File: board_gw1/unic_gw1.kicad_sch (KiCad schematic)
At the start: 112 parts, among them Q1 2N7002, Q10 2N7002, Q11 2N7002, Q12 2N7002, Q13 2N7002, Q14 2N7002, Q15 2N7002, Q16 2N7002, Q17 2N7002, Q18 2N7002, Q19 2N7002, Q2 2N7002, Q20 2N7002, Q21 2N7002, Q22 2N7002, Q23 2N7002, Q24 2N7002, Q25 2N7002, Q26 2N7002, Q27 2N7002, Q28 2N7002, Q29 2N7002, Q3 2N7002, Q30 2N7002, Q31 2N7002, Q32 2N7002, Q33 2N7002, Q34 2N7002, Q35 2N7002, Q36 2N7002, Q37 2N7002, Q38 2N7002, Q39 2N7002, Q4 2N7002, Q40 2N7002, Q5 2N7002, Q6 2N7002, Q7 2N7002, Q8 2N7002, Q9 2N7002, U1 GW1N-LV9QN88C6_I5_, U2 LM3480-3.3, U3 AP2202K-ADJ, U4 APS6404L-3SQR-ZR, U6 AP62150Z6, U7 W25Q16JVUXIQ, X1 27MHz

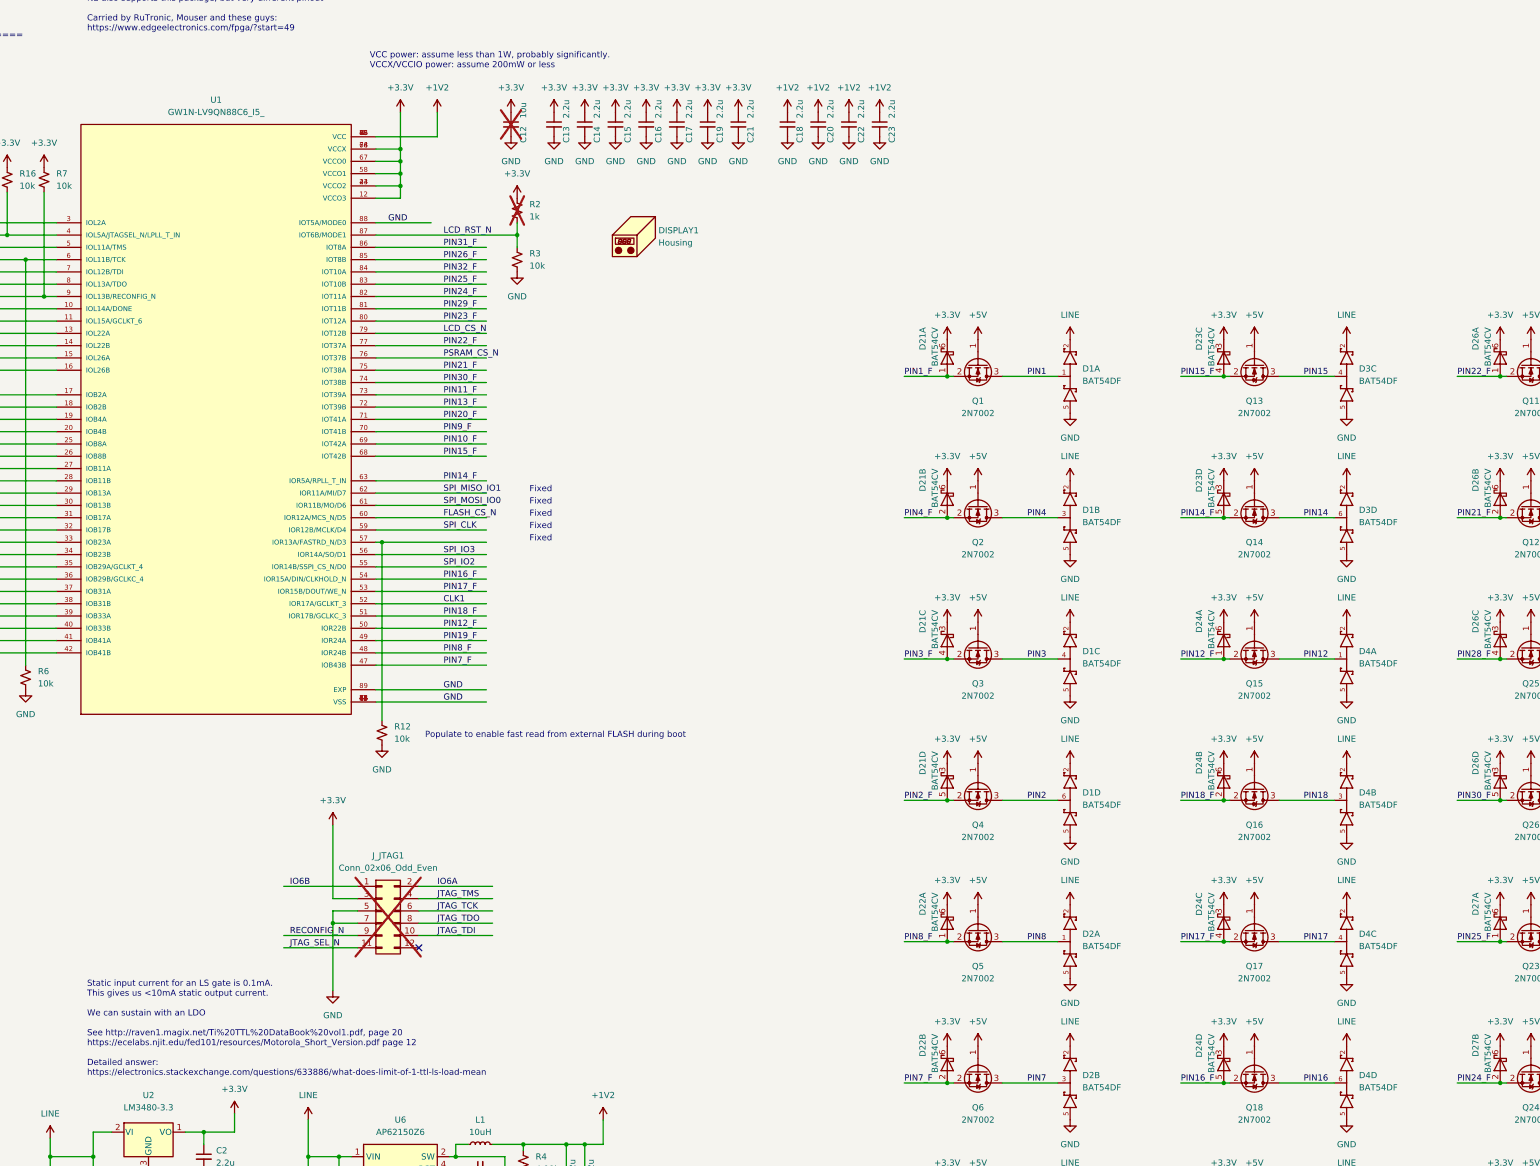
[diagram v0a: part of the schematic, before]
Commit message: Some updated to UNIC GW1 based on post-release learnings.
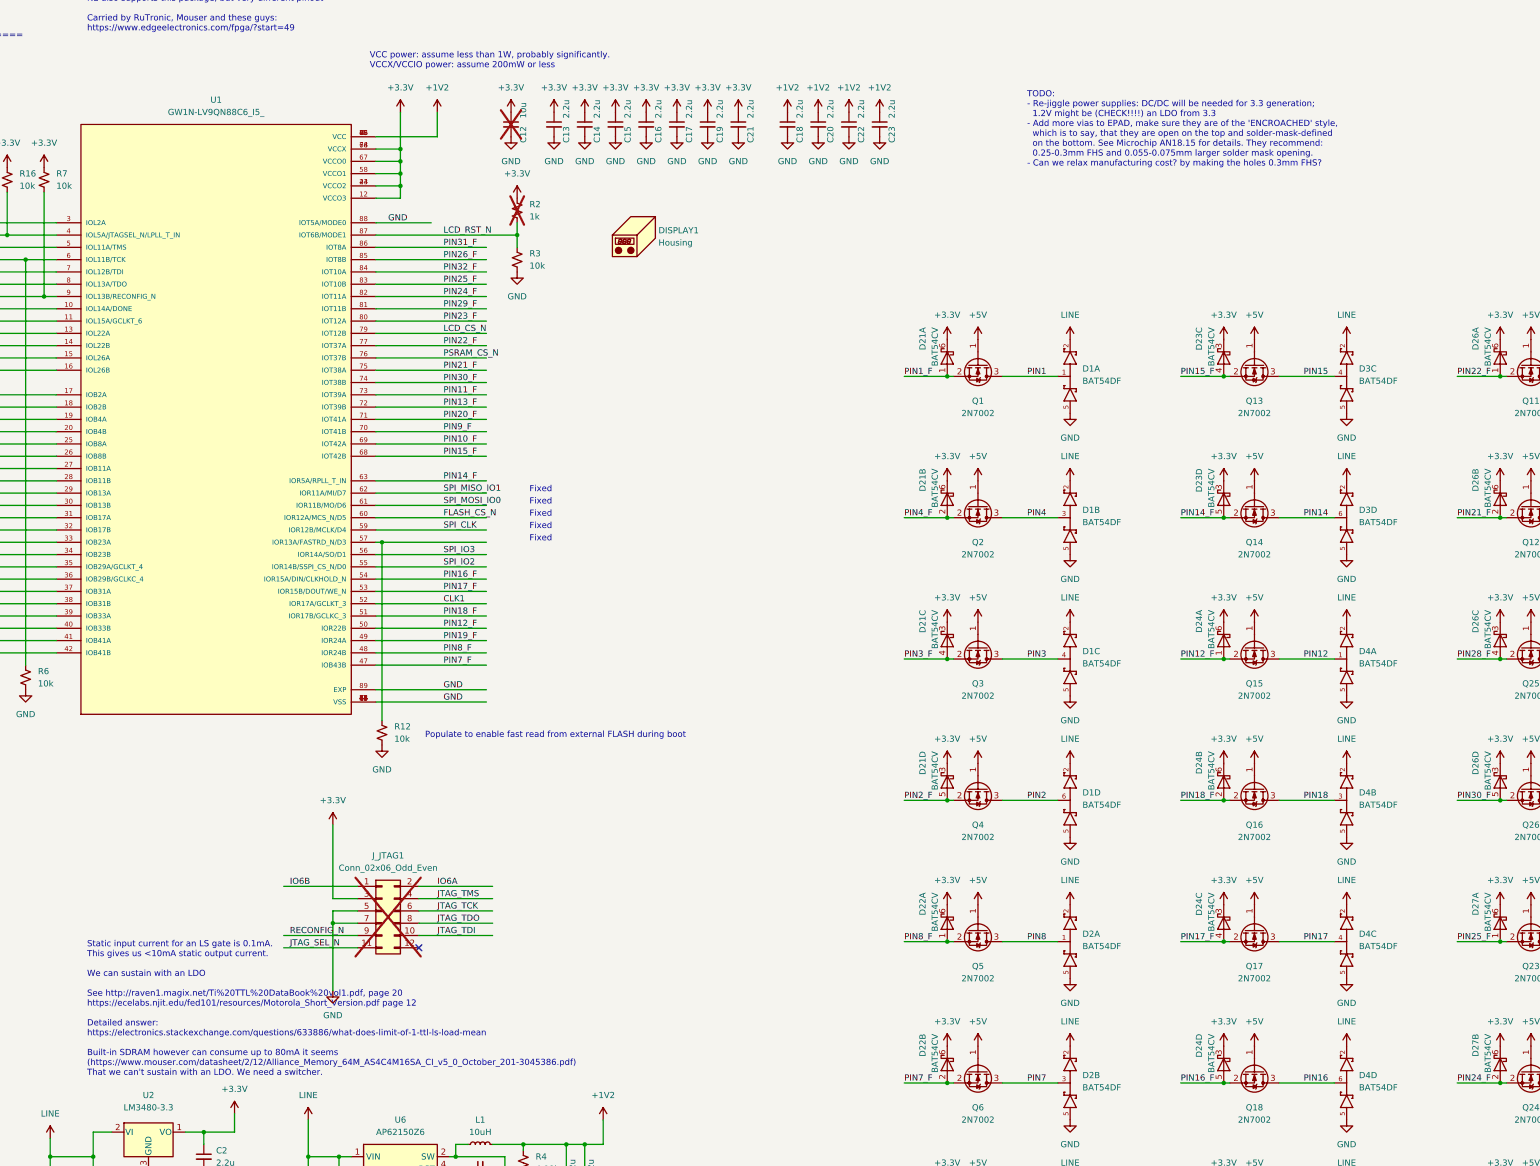
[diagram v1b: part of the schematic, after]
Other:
- note added: "Static input current for an LS gate is 0.1mA. This gives us <10mA static output current. We can sustain with an LDO See http://raven1.magix.net/Ti%20TTL%20DataBook%20vol1.pdf, page 20 https://ecelabs.njit.edu/fed101/resources/Motorola_Short_Version.pdf page 12 Detailed answer: https://electronics.stackexchange.com/questions/633886/what-does-limit-of-1-ttl-ls-load-mean Built-in SDRAM however can c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"
- note added: "TODO: - Re-jiggle power supplies: DC/DC will be needed for 3.3 generation; 1.2V might be (CHECK!!!!) an LDO from 3.3 - Add more vias to EPAD, make sure they are of the 'ENCROACHED' style, which is to say, that they are open on the top and solder-mask-defined on the bottom. See Microchip AN18.15 for details. They recommend: 0.25-0.3mm FHS and 0.055-0.075mm larger solder mask opening. - Can we rela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"
- note removed: "Static input current for an LS gate is 0.1mA. This gives us <10mA static output current. We can sustain with an LDO See http://raven1.magix.net/Ti%20TTL%20DataBook%20vol1.pdf, page 20 https://ecelabs.njit.edu/fed101/resources/Motorola_Short_Version.pdf page 12 Detailed answer: https://electronics.stackexchange.com/questions/633886/what-does-limit-of-1-ttl-ls-load-mean"
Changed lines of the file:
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@@
+    (effects (font (size 1.27 1.27)) (justify left bottom))
+  )
+  (text "TODO:\n- Re-jiggle power supplies: DC/DC will be needed for 3.3 generation;\n  1.2V might be (CHECK!!!!) an LDO from 3.3\n- Add more vias to EPAD, make sure they are of the 'ENCROACHED' style,\n  which is to say, that they are open on the top and solder-mask-defined\n  on the bottom. See Microchip AN18.15 for details. They recommend:\n  0.25-0.3mm FHS and 0.055-0.075mm larger solder mask opening.\n- Can we relax manufacturing cost? by making the holes 0.3mm FHS?"
+    (at 334.01 57.15 0)
     (effects (font (size 1.27 1.27)) (justify left bottom))
   )
@@
     (effects (font (size 1.27 1.27)) (justify left bottom))
   )
-  (text "Static input current for an LS gate is 0.1mA.\nThis gives us <10mA static output current.\n\nWe can sustain with an LDO\n\nSee http://raven1.magix.net/Ti%20TTL%20DataBook%20vol1.pdf, page 20\nhttps://ecelabs.njit.edu/fed101/resources/Motorola_Short_Version.pdf page 12\n\nDetailed answer:\nhttps://electronics.stackexchange.com/questions/633886/what-does-limit-of-1-ttl-ls-load-mean"
+  (text "Static input current for an LS gate is 0.1mA.\nThis gives us <10mA static output current.\n\nWe can sustain with an LDO\n\nSee http://raven1.magix.net/Ti%20TTL%20DataBook%20vol1.pdf, page 20\nhttps://ecelabs.njit.edu/fed101/resources/Motorola_Short_Version.pdf page 12\n\nDetailed answer:\nhttps://electronics.stackexchange.com/questions/633886/what-does-limit-of-1-ttl-ls-load-mean\n\nBuilt-in SDRAM however can consume up to 80mA it seems\n(https://www.mouser.com/datasheet/2/12/Alliance_Memory_64M_AS4C4M16SA_CI_v5_0_October_201-3045386.pdf)\nThat we can't sustain with an LDO. We need a switcher."
     (at 139.7 245.11 0)
     (effects (font (size 1.27 1.27)) (justify left bottom))
@@
       (effects (font (size 1.27 1.27)) (justify bottom) hide)
     )
-    (property "Description" "\nVolatile SRAM based and non-volatile flash-based field-programmable gate array (FPGA) technology\n" (at 166.37 109.22 0)
+    (property "Description" "Volatile SRAM based and non-volatile flash-based field-programmable gate array (FPGA) technology" (at 166.37 109.22 0)
       (effects (font (size 1.27 1.27)) (justify bottom) hide)
     )

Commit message: Updated board file; started cover CAD.
This checkin marks the hopefully complete V1.0 design for the form-factor
board.

It also contains the first (incomplete) iteration of the cover design.
It has a bunch of interference with components on the PCB which
needs to be cleaned. It's also unclear if snaps have to be 1.5mm thick.
Seems excessive. Finally, I don't think the OLED display can even survive
such stiff snaps. But it at least a start.
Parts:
- removed C12: 10u, Capacitor_SMD:C_0805_2012Metric_Pad1.18x1.45mm_HandSolder, symbol Device:C_Small
- removed U2: LM3480-3.3, Package_TO_SOT_SMD:SOT-23, symbol Regulator_Linear:LM3480-3.3
- added C10: 2.2u, Capacitor_SMD:C_0402_1005Metric_Pad0.74x0.62mm_HandSolder, symbol Device:C_Small
- added Q41: 2N7002, UNIC:SOT-883, symbol Transistor_FET:2N7002
- added R17: 100k, Resistor_SMD:R_0402_1005Metric_Pad0.72x0.64mm_HandSolder, symbol Device:R_Small_US
- added U5: MIC5504-1.2YM5, Package_TO_SOT_SMD:SOT-23-5, symbol Regulator_Linear:MIC5504-1.2YM5
- C1, C11, C13, C14, C15, C16, C17, C18, C19, C2, C20, C21, C22, C23, C3, C4, C6, C9: manf (none) -> YAGEO
- C5, C7, C8: manf (none) -> Samsung Electro-Mechanics
- D1, D11, D2, D3, D4, D5, D6, D7, D8, D9: manf (none) -> SMC Diode Solutions
- D21, D22, D23, D24, D25, D26, D27, D28, D29, D30: manf (none) -> Nexperia USA Inc.
- DISPLAY1: manf (none) -> Crystalfontz America, Inc.; now not fitted
- J_DISPLAY1: manf (none) -> Cvilux USA
- J_EXT1: manf (none) -> Molex
- J_JTAG1: manf (none) -> Amphenol ICC (FCI)
- L1: manf (none) -> TAI-TECH Advanced Electronics Co., Ltd.
- LED_DONE1: manf (none) -> ChromeLED
- Q1, Q10, Q11, Q12, Q13, Q14, Q15, Q16, Q17, Q18, Q19, Q2, Q20, Q21, Q22, Q23, Q24, Q25, Q26, Q27, Q28, Q29, Q3, Q30, Q31, Q32, Q33, Q34, Q35, Q36, Q37, Q38, Q39, Q4, Q40, Q5, Q6, Q7, Q8, Q9: manf (none) -> Micro Commercial Co
- R1, R10, R11, R12, R13, R16, R2, R3, R5, R6, R7, R8, R9: manf (none) -> Bourns Inc.
- R14: manf (none) -> Bourns Inc.; manf# ERJ-2RKF4991X -> CR0402-FX-4991GLF; now not fitted
- R15: manf (none) -> Bourns Inc.; now not fitted
- R4: value 4.99k -> 31.6k; manf (none) -> Bourns Inc.; manf# ERJ-2RKF4991X -> CR0402-FX-3162GLF
- SOCKET1: manf (none) -> Batten & Allen Limited
- U1: manf (none) -> GOWIN Semiconductor; manf# GW1N-LV9QN88C6/I5/ -> GW1N-LV9QN88C6/I5
- U3: value AP2202K-ADJ -> MIC5203-3.3BM5; manf (none) -> Microchip Technology; manf# AP2202K-ADJTRE1 -> MIC5203-3.3YM5-TR
- U4: manf (none) -> AP Memory
- U6: manf (none) -> Diodes Incorporated
- U7: manf (none) -> Winbond Electronics
- X1: manf (none) -> Jauch Quartz
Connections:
- net +1V2: now also C2.1, U5.5 (VOUT); no longer C7.1, C8.1, L1.2, R4.1
- net +3V3: now also C7.1, C8.1, L1.2, R4.1, C10.1, U5.1 (VIN), U5.3 (EN); no longer C2.1
- net GND: now also C10.2, Q41.2 (S), U5.2 (GND); no longer U3.2 (GND)
- net LINE: now also R17.1
- new net: Q41.1 (G), Q41.3 (D), R17.2, U3.2 (GND)
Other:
- note added: "Even though we could sustain the I/O current through an LDO, the SDRAM consumes and extra 80mA or so. Better use a switcher for 3.3V."
- note added: "TODO: - Add more vias to EPAD, make sure they are of the 'ENCROACHED' style, which is to say, that they are open on the top and solder-mask-defined on the bottom. See Microchip AN18.15 for details. They recommend: 0.25-0.3mm FHS and 0.055-0.075mm larger solder mask opening. ... I don't think KiCAD can do this kind of thing. - Can we relax manufacturing cost? by making the holes 0.3mm FHS?"
- note removed: "5V is trimmed to 4.5V"
- note removed: "Static input current for an LS gate is 0.1mA. This gives us <10mA static output current. We can sustain with an LDO See http://raven1.magix.net/Ti%20TTL%20DataBook%20vol1.pdf, page 20 https://ecelabs.njit.edu/fed101/resources/Motorola_Short_Version.pdf page 12 Detailed answer: https://electronics.stackexchange.com/questions/633886/what-does-limit-of-1-ttl-ls-load-mean Built-in SDRAM however can c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"
- note removed: "TODO: - Re-jiggle power supplies: DC/DC will be needed for 3.3 generation; 1.2V might be (CHECK!!!!) an LDO from 3.3 - Add more vias to EPAD, make sure they are of the 'ENCROACHED' style, which is to say, that they are open on the top and solder-mask-defined on the bottom. See Microchip AN18.15 for details. They recommend: 0.25-0.3mm FHS and 0.055-0.075mm larger solder mask opening. - Can we rela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"
- moved on the sheet: C2, C3, U3

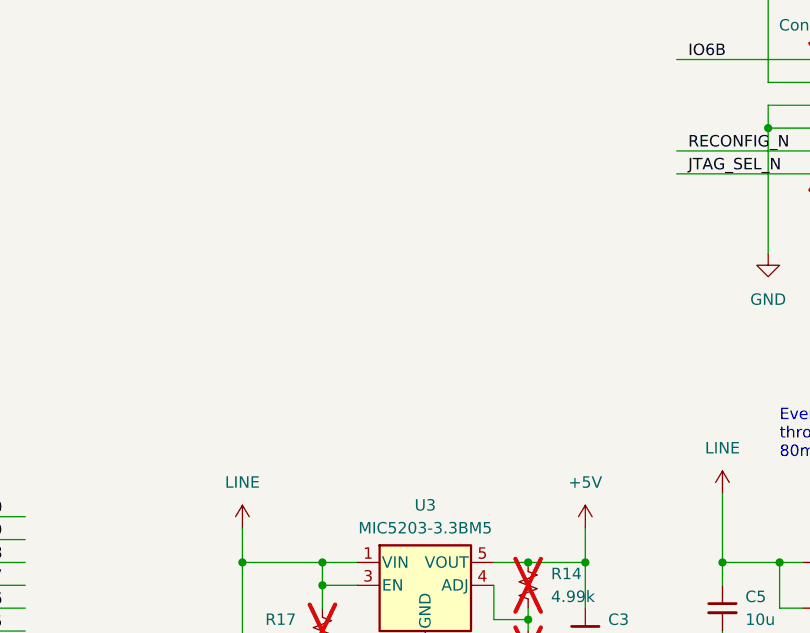
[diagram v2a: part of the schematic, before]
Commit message: Added test-points, edge clearance, some cleanup.
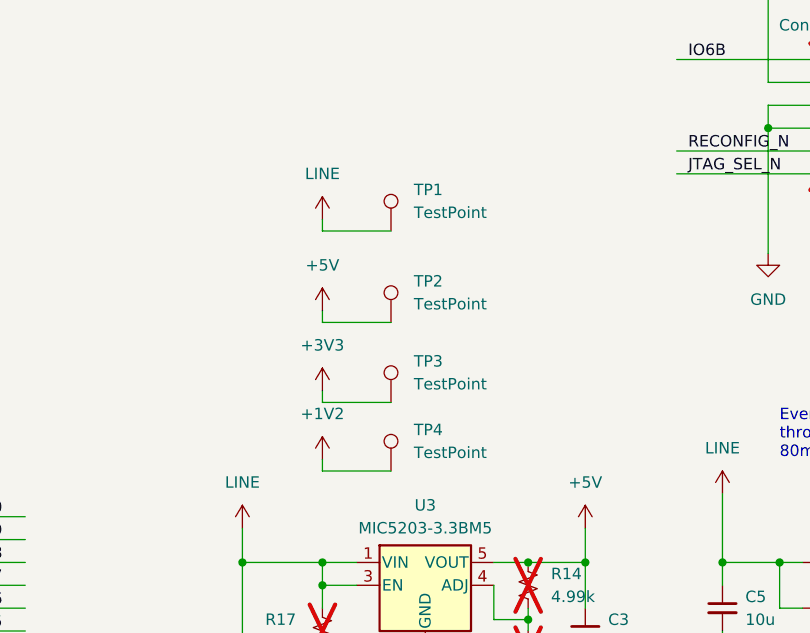
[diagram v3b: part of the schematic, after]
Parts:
- added TP1, TP2, TP3, TP4: TestPoint, TestPoint:TestPoint_Pad_D2.0mm, symbol Connector:TestPoint
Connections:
- net +1V2: now also TP4.1
- net +3V3: now also TP3.1
- net +5V: now also TP2.1
- net LINE: now also TP1.1

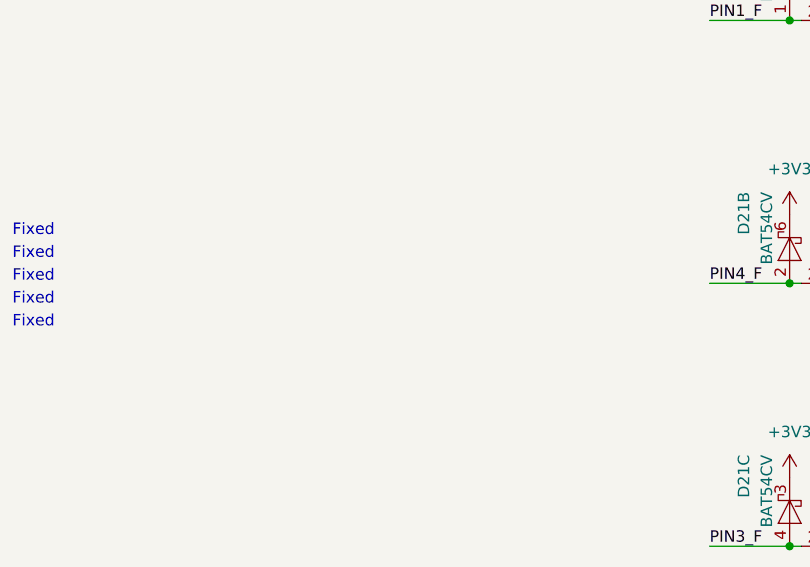
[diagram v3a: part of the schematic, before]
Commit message: Added fiducials and some other flourishes.
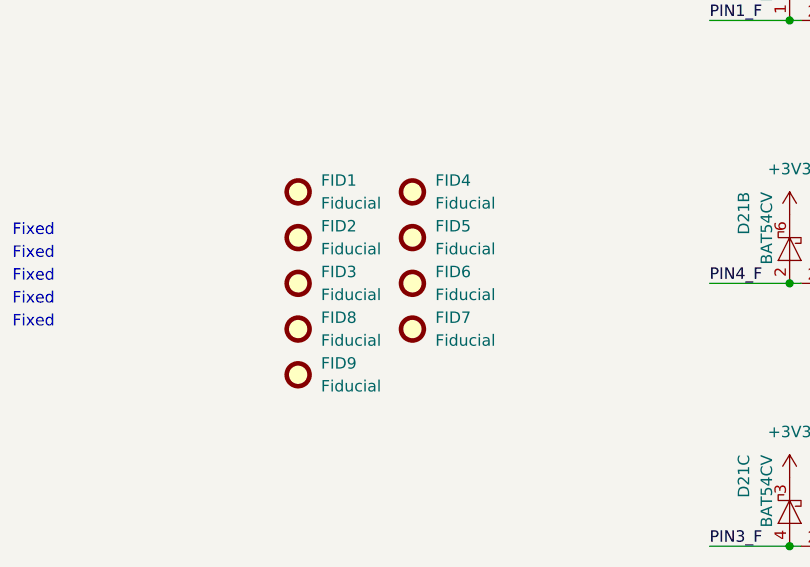
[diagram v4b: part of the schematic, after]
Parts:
- added FID1, FID2, FID3, FID4, FID5, FID6, FID7, FID8, FID9: Fiducial, Fiducial:Fiducial_0.5mm_Mask1mm, symbol Mechanical:Fiducial

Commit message: Lots of (local) footprint cleanup and readying for board release.
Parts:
- C1, C10, C11, C13, C14, C15, C16, C17, C18, C19, C2, C20, C21, C22, C23, C3, C4, C6, C9: footprint Capacitor_SMD:C_0402_1005Metric_Pad0.74x0.62mm_HandSolder -> UNIC:C_0402_1005Metric_Pad0.74x0.62mm_HandSolder
- C5, C7, C8: footprint Capacitor_SMD:C_0805_2012Metric_Pad1.18x1.45mm_HandSolder -> UNIC:C_0805_2012Metric_Pad1.18x1.45mm_HandSolder
- D21, D22, D23, D24, D25, D26, D27, D28, D29, D30: footprint Package_TO_SOT_SMD:SOT-666 -> UNIC:SOT-666
- FID1, FID2, FID3, FID4, FID5, FID6, FID7, FID8, FID9: footprint Fiducial:Fiducial_0.5mm_Mask1mm -> UNIC:Fiducial_0.5mm_Mask1mm
- L1: footprint Inductor_SMD:L_1008_2520Metric_Pad1.43x2.20mm_HandSolder -> UNIC:L_1008_2520Metric_Pad1.43x2.20mm_HandSolder
- LED_DONE1: footprint LED_SMD:LED_0402_1005Metric_Pad0.77x0.64mm_HandSolder -> UNIC:LED_0402_1005Metric_Pad0.77x0.64mm_HandSolder
- R1, R10, R11, R12, R13, R14, R15, R16, R17, R2, R3, R4, R5, R6, R7, R8, R9: footprint Resistor_SMD:R_0402_1005Metric_Pad0.72x0.64mm_HandSolder -> UNIC:R_0402_1005Metric_Pad0.72x0.64mm_HandSolder
- TP1, TP2, TP3, TP4: footprint TestPoint:TestPoint_Pad_D2.0mm -> UNIC:TestPoint_Pad_D2.0mm
- U3, U5: footprint Package_TO_SOT_SMD:SOT-23-5 -> UNIC:SOT-23-5
- U6: footprint Package_TO_SOT_SMD:SOT-563 -> UNIC:SOT-563
